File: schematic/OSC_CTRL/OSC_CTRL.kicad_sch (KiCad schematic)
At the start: 35 parts, among them J1 ASDR_CTRL, J2 WAVE_CTRL, J4 Conn_01x02, U3 CD74HC4067SM, U4 CD74HC4067SM

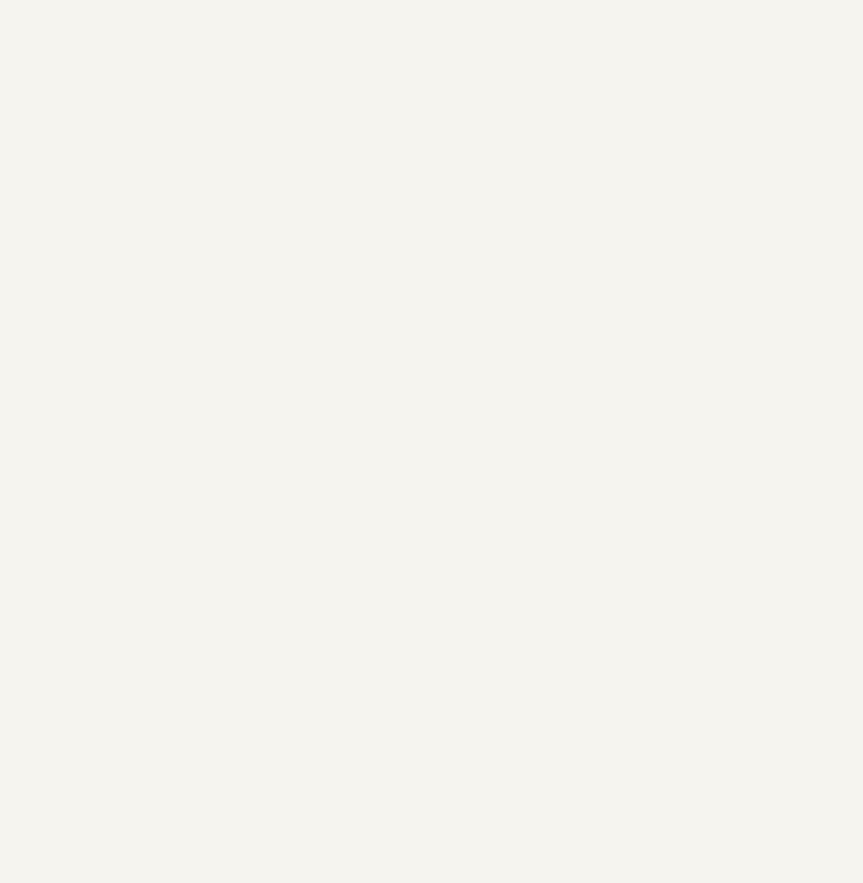
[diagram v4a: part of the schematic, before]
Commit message: adding new rev of apm board with new routing and power management
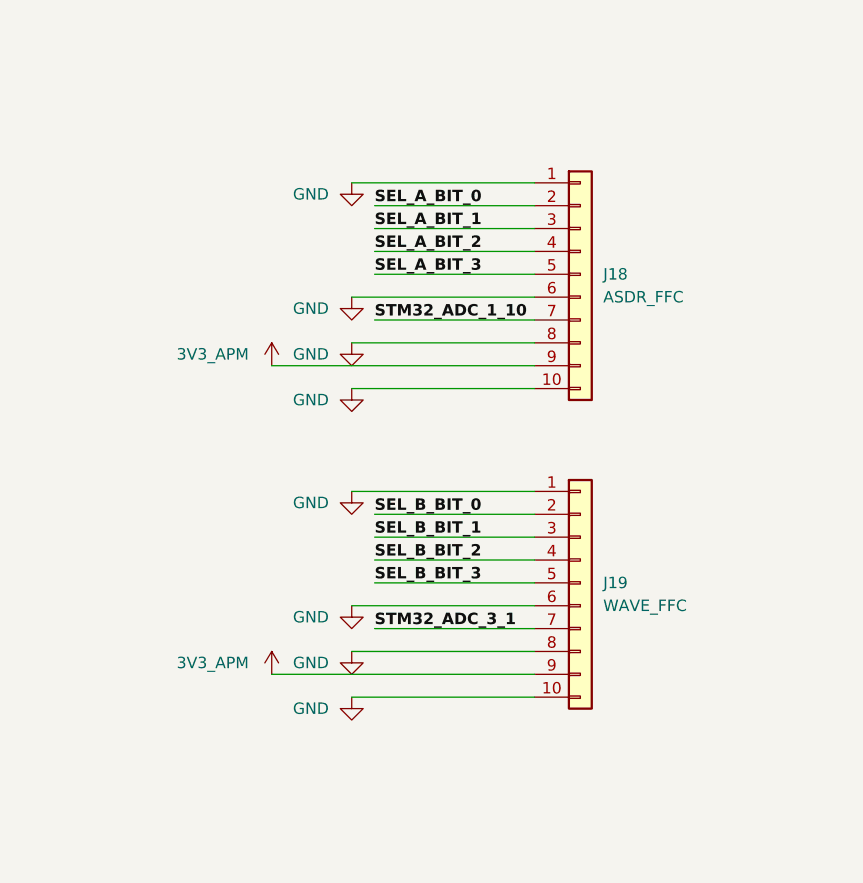
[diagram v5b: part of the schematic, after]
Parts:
- added J18: ASDR_FFC, Connector_FFC-FPC:Hirose_FH12-10S-0.5SH_1x10-1MP_P0.50mm_Horizontal, symbol Connector_Generic:Conn_01x10
- added J19: WAVE_FFC, Connector_FFC-FPC:Hirose_FH12-10S-0.5SH_1x10-1MP_P0.50mm_Horizontal, symbol Connector_Generic:Conn_01x10
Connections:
- net GND: now also J18.1 (Pin_1), J18.10 (Pin_10), J18.6 (Pin_6), J18.8 (Pin_8), J19.1 (Pin_1), J19.10 (Pin_10), J19.6 (Pin_6), J19.8 (Pin_8)
- net SEL_A_BIT_0: now also J18.2 (Pin_2)
- net SEL_A_BIT_1: now also J18.3 (Pin_3)
- net SEL_A_BIT_2: now also J18.4 (Pin_4)
- net SEL_A_BIT_3: now also J18.5 (Pin_5)
- net SEL_B_BIT_0: now also J19.2 (Pin_2)
- net SEL_B_BIT_1: now also J19.3 (Pin_3)
- net SEL_B_BIT_2: now also J19.4 (Pin_4)
- net SEL_B_BIT_3: now also J19.5 (Pin_5)
- net STM32_ADC_1_10: now also J18.7 (Pin_7)
- net STM32_ADC_3_1: now also J19.7 (Pin_7)
- new net 3V3_APM: J18.9 (Pin_9), J19.9 (Pin_9)

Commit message: adding 20p ffc instead on OSC CTRL board. rerouting it, then doing APM side
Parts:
- removed J18: ASDR_FFC, Connector_FFC-FPC:Hirose_FH12-10S-0.5SH_1x10-1MP_P0.50mm_Horizontal, symbol Connector_Generic:Conn_01x10
- removed J19: WAVE_FFC, Connector_FFC-FPC:Hirose_FH12-10S-0.5SH_1x10-1MP_P0.50mm_Horizontal, symbol Connector_Generic:Conn_01x10
- added J5: OSC_CTRL, my_footprints:GCT_FFC2B28-20-G, symbol FFC2B28-20-G:FFC2B28-20-G
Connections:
- net 3V3_APM: now also J5.19, J5.9
- net GND: now also J5.1, J5.16, J5.18, J5.20, J5.6, J5.8, J5.S1 (SHIELD), J5.S2 (SHIELD)
- net SEL_A_BIT_0: now also J5.2
- net SEL_A_BIT_1: now also J5.3
- net SEL_A_BIT_2: now also J5.4
- net SEL_A_BIT_3: now also J5.5
- net SEL_B_BIT_0: now also J5.12
- net SEL_B_BIT_1: now also J5.13
- net SEL_B_BIT_2: now also J5.14
- net SEL_B_BIT_3: now also J5.15
- net STM32_ADC_1_10: now also J5.7
- net STM32_ADC_3_1: now also J5.17
- new net: J5.10, J5.11
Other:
- note added: "Each pad is capable of supplying 0.5A"
- note added: "WAVE_SEL"

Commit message: gonna try autorouting the whol eboard?
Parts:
- removed J4: Conn_01x02, Connector_PinSocket_2.54mm:PinSocket_1x02_P2.54mm_Vertical_SMD_Pin1Left, symbol Connector_Generic:Conn_01x02
- added TP3: FPC_3V3_TP, TestPoint:TestPoint_Pad_D1.0mm, symbol Connector:TestPoint
- added TP4: FPC_GND_TP, TestPoint:TestPoint_Pad_D1.0mm, symbol Connector:TestPoint
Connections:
- net 3V3_APM is gone; now on net 3V3_IN: J5.19, J5.9
- net 3V3_IN: now also TP3.1
- net GND: now also TP4.1
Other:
- moved on the sheet: C2, D1, F2, PWR1, R39

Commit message: maybe not the entire board. bit of a pain
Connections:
- net GND: now also J5.10, J5.11
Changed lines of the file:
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@@
 	)
 	(junction
+		(at 377.19 154.94)
+		(diameter 0)
+		(color 0 0 0 0)
+	)
+	(junction
 		(at 226.06 123.19)
 		(diameter 0)
@@
 	(wire
 		(pts
-			(xy 377.19 153.67) (xy 377.19 156.21)
+			(xy 377.19 153.67) (xy 377.19 154.94)
 		)
 		(stroke
@@
 	(wire
 		(pts
+			(xy 375.92 154.94) (xy 377.19 154.94)
+		)
+		(stroke
+			(width 0)
+			(type default)
+		)
+	)
+	(wire
+		(pts
 			(xy 196.85 138.43) (xy 213.36 138.43)
 		)
@@
 	(wire
 		(pts
+			(xy 377.19 154.94) (xy 377.19 156.21)
+		)
+		(stroke
+			(width 0)
+			(type default)
+		)
+	)
+	(wire
+		(pts
 			(xy 96.52 157.48) (xy 96.52 165.1)
 		)
@@
 					(unit 1)
 				)
+			)
+		)
+	)
+	(symbol
+		(lib_id "power:GND")
+		(at 375.92 154.94 0)
+		(unit 1)
+		(body_style 1)
+		(exclude_from_sim no)
+		(in_bom yes)
+		(on_board yes)
+		(in_pos_files yes)
+		(dnp no)
+		(fields_autoplaced yes)
+		(property "Reference" "#PWR0130"
+			(at 375.92 161.29 0)
+			(hide yes)
+			(show_name no)
+			(do_not_autoplace no)
+			(effects
+				(font
+					(size 1.27 1.27)
+				)
+			)
+		)
+		(property "Value" "GND"
+			(at 373.38 156.2099 0)
+			(show_name no)
+			(do_not_autoplace no)
+			(effects
+				(font
+					(size 1.27 1.27)
+				)
+				(justify right)
+			)
+		)
+		(property "Footprint" ""
+			(at 375.92 154.94 0)
+			(hide yes)
+			(show_name no)
+			(do_not_autoplace no)
+			(effects
+				(font
+					(size 1.27 1.27)
+				)
+			)
+		)
+		(property "Datasheet" ""
+			(at 375.92 154.94 0)
+			(hide yes)
+			(show_name no)
+			(do_not_autoplace no)
+			(effects
+				(font
+					(size 1.27 1.27)
+				)
+			)
+		)
+		(property "Description" "Power symbol creates a global label with name \"GND\" , ground"
+			(at 375.92 154.94 0)
+			(hide yes)
+			(show_name no)
+			(do_not_autoplace no)
+			(effects
+				(font
+					(size 1.27 1.27)
+				)
+			)
+		)
+		(pin "1"
+		)
+		(instances
+			(project "OSC_CTRL"
+				(path "/f48c9b16-466a-451c-a18e-f0696896ad19"
+					(reference "#PWR0130")
+					(unit 1)
+				)
